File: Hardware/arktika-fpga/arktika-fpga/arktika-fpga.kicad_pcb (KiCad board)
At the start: 2 copper layers, 126 parts

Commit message: Added fuses library to project. Minor changes
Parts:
- UPER1: moved to B.Cu
- moved CPER4 325.4 mm to (64.2, 39.6), turned to 270 degrees
- moved CPER3 323.7 mm to (65.7, 39.6), turned to 270 degrees
- moved CPER1 300.4 mm to (95.5, 44.7)
- moved CPER2 300.4 mm to (92.9, 49.2)
- moved RPER1 300.4 mm to (92.8, 38.3)
- moved FUSB2 293.1 mm to (60.7, 44.5), turned to 90 degrees
- moved DUSB2 290.5 mm to (87.6, 43.6)
- moved LP1_3 153.6 mm to (49.1, 102.9), turned to 90 degrees
- moved CP6_1 153.1 mm to (48.6, 89.8), turned to 90 degrees
- moved CP1_2 149.8 mm to (50.9, 89.8), turned to 90 degrees
- moved DP3 146.5 mm to (53.6, 97.3), turned to 90 degrees
- moved CP4_1 146.2 mm to (53.5, 92.5), turned to 90 degrees
- moved CP4_3 143.2 mm to (56.0, 97.5), turned to 90 degrees
- moved CP7 142.9 mm to (55.9, 92.5), turned to 90 degrees
- moved RP2 141.0 mm to (58.3, 104.5), turned to 90 degrees
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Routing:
- net Net-(FUSB2-Pad2): track 0.00 -> 4.83 mm
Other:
- net class Default: clearance 0.2 -> 0.05
- rule trace_clearance: 0.2 -> 0.05
- rule trace_min: 0.2 -> 0.125

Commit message: Misc schematic changes. Preliminary layout almost complete
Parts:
- removed CP6: 10n, Capacitors_SMD:C_0603_HandSoldering
- removed JP1: Conn_01x03, Pin_Headers:Pin_Header_Straight_1x03_Pitch2.54mm
- added CP7_1: 10n, Capacitor_SMD:C_0603_1608Metric_Pad1.05x0.95mm_HandSolder, F.Cu at (187.4, 100.8)
- added CP7_2: 10n, Capacitor_SMD:C_0603_1608Metric_Pad1.05x0.95mm_HandSolder, F.Cu at (159.5, 84.8)
- added CP7_3: 10n, Capacitor_SMD:C_0603_1608Metric_Pad1.05x0.95mm_HandSolder, F.Cu at (177.4, 107.2)
- added JPUP6_2: SolderJumper_2_Open, Jumper:SolderJumper-2_P1.3mm_Open_RoundedPad1.0x1.5mm, F.Cu at (157.5, 103.3)
- added JUP6_1: SolderJumper_2_Open, Jumper:SolderJumper-2_P1.3mm_Open_RoundedPad1.0x1.5mm, F.Cu at (157.5, 100.8)
- A1: footprint Modules:Arduino_UNO_R3 -> Module:Arduino_UNO_R3_WithMountingHoles
- CCP5_2, CP1_2, CP1_3, CP2_2, CP2_3, CP3_2, CP3_3, CP4_2, CP4_3, CP5_3, CP6_2, CP6_3, CUP2, CUP4, CUP7, CUP9: footprint Capacitors_SMD:C_0603_HandSoldering -> Capacitor_SMD:C_0603_1608Metric_Pad1.05x0.95mm_HandSolder; moved to B.Cu
- CIN1, CP1_1, CP2_1, CP3_1, CP4_1, CP5_1, CP6_1, CPER1, CPER2, CPER3, CPER4, CUP1, CUP10, CUP11, CUP3, CUP5, CUP6, CUP8_1, CUP8_2: footprint Capacitors_SMD:C_0603_HandSoldering -> Capacitor_SMD:C_0603_1608Metric_Pad1.05x0.95mm_HandSolder
- CP10_1: renamed from CP9_1; footprint Capacitors_SMD:C_0603_HandSoldering -> Capacitor_SMD:C_0603_1608Metric_Pad1.05x0.95mm_HandSolder
- CP10_2: renamed from CP10_1; footprint Capacitors_SMD:C_0603_HandSoldering -> Capacitor_SMD:C_0603_1608Metric_Pad1.05x0.95mm_HandSolder
- CP11_1: renamed from CP9_2; footprint Capacitors_SMD:C_0603_HandSoldering -> Capacitor_SMD:C_0603_1608Metric_Pad1.05x0.95mm_HandSolder
- CP11_2: renamed from CP10_2; footprint Capacitors_SMD:C_0603_HandSoldering -> Capacitor_SMD:C_0603_1608Metric_Pad1.05x0.95mm_HandSolder
- CP8: renamed from CP7; footprint Capacitors_SMD:C_0603_HandSoldering -> Capacitor_SMD:C_0603_1608Metric_Pad1.05x0.95mm_HandSolder
- CP9: renamed from CP8; footprint Capacitors_SMD:C_0603_HandSoldering -> Capacitor_SMD:C_0603_1608Metric_Pad1.05x0.95mm_HandSolder
- D0, D1, D2, D3, D4, D5, D6, D7, DP3, DUP1, DUP2, DUP3: footprint LEDs:LED_0603_HandSoldering -> LED_SMD:LED_0603_1608Metric_Pad1.05x0.95mm_HandSolder
- DP1, DP2: footprint Diodes_SMD:D_SMA-SMB_Universal_Handsoldering -> Diode_SMD:D_SMA-SMB_Universal_Handsoldering
- DUSB1, DUSB2: footprint TO_SOT_Packages_SMD:SOT-143 -> Package_TO_SOT_SMD:SOT-143
- FP1, FUSB1, FUSB2: footprint Fuses:Fuse_1812_4532Metric -> Fuse:Fuse_1812_4532Metric_Pad1.30x3.40mm_HandSolder
- JP2: moved to B.Cu
- JUP9: footprint Pin_Headers:Pin_Header_Straight_1x07_Pitch2.54mm -> Connector_PinHeader_2.54mm:PinHeader_1x07_P2.54mm_Horizontal
- LP1_1: footprint Inductors_SMD:L_1206_HandSoldering -> Inductor_SMD:L_1206_3216Metric_Pad1.42x1.75mm_HandSolder
- LP1_2, LP1_3: footprint Inductors_SMD:L_1206_HandSoldering -> Inductor_SMD:L_1206_3216Metric_Pad1.42x1.75mm_HandSolder; moved to B.Cu
- PMODA_1, PMODA_2: footprint Pin_Headers:Pin_Header_Angled_2x06_Pitch2.54mm -> Connector_PinHeader_2.54mm:PinHeader_2x06_P2.54mm_Horizontal
- PMODB_1, PMODB_2: footprint Pin_Headers:Pin_Header_Angled_2x04_Pitch2.54mm -> Connector_PinHeader_2.54mm:PinHeader_2x04_P2.54mm_Horizontal
- PMODC_1, PMODC_2: footprint Pin_Headers:Pin_Header_Angled_1x06_Pitch2.54mm -> Connector_PinHeader_2.54mm:PinHeader_1x06_P2.54mm_Horizontal
- PSH0, PSH1, PSH2, PSH3: footprint Buttons_Switches_SMD:SW_SPST_PTS645 -> Button_Switch_SMD:SW_SPST_PTS645
- RP1_1, RP1_2, RP2, RPER1, RUP1, RUP2, RUP3, RUP7_1, RUP8: footprint Resistors_SMD:R_0603_HandSoldering -> Resistor_SMD:R_0603_1608Metric_Pad1.05x0.95mm_HandSolder
- RPER2: footprint Resistors_SMD:R_Array_Convex_4x0603 -> Resistor_SMD:R_Array_Convex_4x0603; moved to B.Cu
- RPER3, RPER4, RPER5, RPER6: footprint Resistors_SMD:R_Array_Convex_4x0603 -> Resistor_SMD:R_Array_Convex_4x0603
- RUP4, RUP5, RUP6, RUP7, RUP7_2, RUP7_3, RUP7_4: footprint Resistors_SMD:R_0603_HandSoldering -> Resistor_SMD:R_0603_1608Metric_Pad1.05x0.95mm_HandSolder; moved to B.Cu
- SW[7..0]1: footprint Buttons_Switches_SMD:SW_DIP_x8_W8.61mm_Slide_LowProfile -> Button_Switch_SMD:SW_DIP_SPSTx08_Slide_6.7x21.88mm_W8.61mm_P2.54mm_LowProfile
- UP1: footprint TO_SOT_Packages_SMD:SOT-223-3_TabPin2 -> Package_TO_SOT_SMD:SOT-223-3_TabPin2
- UP2, UP3: footprint TO_SOT_Packages_SMD:SOT-23 -> Package_TO_SOT_SMD:SOT-23; moved to B.Cu
- UPER1: footprint Housings_DFN_QFN:QFN-28-1EP_4x4mm_Pitch0.4mm -> Package_DFN_QFN:QFN-28-1EP_4x4mm_P0.4mm_EP2.6x2.6mm; moved to F.Cu
- UPER2: footprint Housings_SOIC:SOIC-14_3.9x8.7mm_Pitch1.27mm -> Package_SO:SOIC-14_3.9x8.7mm_P1.27mm
- UUP1: footprint Housings_QFP:LQFP-48_7x7mm_Pitch0.5mm -> Package_QFP:LQFP-48-1EP_7x7mm_P0.5mm_EP3.6x3.6mm
- UUP2: footprint TO_SOT_Packages_SMD:SOT-23-6_Handsoldering -> Package_TO_SOT_SMD:SOT-23-6_Handsoldering; moved to B.Cu
- UUP3: footprint Housings_QFP:TQFP-144_20x20mm_Pitch0.5mm -> Package_QFP:TQFP-144_20x20mm_P0.5mm
- UUP4: footprint Housings_SOIC:SOIC-8_3.9x4.9mm_Pitch1.27mm -> Package_SO:SOIC-8_3.9x4.9mm_P1.27mm
- YUP1: footprint Crystals:Crystal_SMD_3225-4pin_3.2x2.5mm_HandSoldering -> Crystal:Crystal_SMD_3225-4Pin_3.2x2.5mm_HandSoldering
- moved CUP5 268.2 mm to (106.8, 113.0), turned to 270 degrees
- moved CUP8_1 264.3 mm to (106.2, 104.0), turned to 90 degrees
- moved CUP10 254.4 mm to (109.4, 124.5), turned to 270 degrees
- moved RPER6 249.4 mm to (149.8, 116.5), turned to 90 degrees
- moved RPER5 247.2 mm to (145.6, 116.5), turned to 90 degrees
- moved CUP6 245.9 mm to (110.3, 102.9), turned to 180 degrees
- moved CUP9 242.6 mm to (105.5, 101.0), turned to 180 degrees
- moved JUP5_1 239.4 mm to (96.8, 100.3)
- moved D7 238.2 mm to (145.2, 123.4)
- moved D6 237.5 mm to (147.6, 123.4)
- moved JUP5_2 236.7 mm to (94.9, 102.5)
- moved D5 236.7 mm to (150.2, 123.4)
- moved D4 235.9 mm to (152.7, 123.4)
- moved D3 235.0 mm to (155.3, 123.4)
- moved RPER4 235.0 mm to (159.1, 132.0)
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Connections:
- net /Power/D+ renamed /D+
- net /Power/D- renamed /D-
- net Net-(JUP5_1-Pad2) renamed /USB AND PROG/D'-
- net Net-(JUP5_2-Pad2) renamed /USB AND PROG/D'+
- net Net-(UUP3-Pad110) renamed /FPGA_IO/EXT1
- A1 pad 10: /FPGA_IO/ADC_CH1 -> ADC_CH1
- A1 pad 11: /FPGA_IO/ADC_CH2 -> ADC_CH2
- A1 pad 12: /FPGA_IO/ADC_CH3 -> ADC_CH3
- A1 pad 9: /FPGA_IO/ADC_CH0 -> ADC_CH0
- CP10_1 pad 2: /Power/GNDPLL0 -> /GNDPLL1
- CP10_2 pad 2: /Power/GNDPLL0 -> /GNDPLL1
- CP11_1 pad 2: /Power/GNDPLL1 -> /GNDPLL0
- CP11_2 pad 2: /Power/GNDPLL1 -> /GNDPLL0
- CUP4 pad 1: Net-(CUP4-Pad1) -> /VCC3V3
- CUP6 pad 1: Net-(CUP4-Pad1) -> /VCC3V3
- DP2 pad 2: Net-(DP2-Pad2) -> /Power/Vbus
- DUP1 pad 1: /USB AND PROG/C9 -> /USB AND PROG/C8'
- DUP2 pad 1: /USB AND PROG/C8 -> /USB AND PROG/C9'
- FUSB1 pad 1: Net-(DP2-Pad2) -> /Power/Vbus
- JUP6 pad 17: Net-(JUP6-Pad17) -> /USB AND PROG/C8'
- JUP6 pad 18: Net-(JUP6-Pad18) -> /USB AND PROG/C9'
- JUP7_1 pad 7: Net-(JUP6-Pad17) -> /USB AND PROG/C8'
- JUP7_1 pad 8: Net-(JUP6-Pad18) -> /USB AND PROG/C9'
- JUP9 pad 1: /USB AND PROG/FLASH_CS -> /USB AND PROG/flash_~RST
- JUP9 pad 2: /USB AND PROG/ICE_SCK -> /USB AND PROG/flash_~WP
- JUP9 pad 3: /USB AND PROG/FLASH_MOSI -> /USB AND PROG/FLASH_MISO
- JUP9 pad 4: /USB AND PROG/FLASH_MISO -> /USB AND PROG/FLASH_MOSI
- JUP9 pad 5: /USB AND PROG/flash_~WP -> /USB AND PROG/ICE_SCK
- JUP9 pad 6: /USB AND PROG/flash_~RST -> /USB AND PROG/FLASH_CS
- PSH0 pad 2: /FPGA_PERIPHS/PSH0 -> /FPGA_IO/PSH0
- PSH1 pad 2: /FPGA_PERIPHS/PSH1 -> /FPGA_IO/PSH1
- PSH2 pad 2: /FPGA_PERIPHS/PSH2 -> /FPGA_IO/PSH2
- PSH3 pad 2: /FPGA_PERIPHS/PSH3 -> /FPGA_IO/PSH3
- RPER2 pad 1: /FPGA_PERIPHS/PSH0 -> /FPGA_IO/PSH0
- RPER2 pad 2: /FPGA_PERIPHS/PSH1 -> /FPGA_IO/PSH1
- RPER2 pad 3: /FPGA_PERIPHS/PSH2 -> /FPGA_IO/PSH2
- RPER2 pad 4: /FPGA_PERIPHS/PSH3 -> /FPGA_IO/PSH3
- RPER3 pad 1: /FPGA_PERIPHS/SW7 -> /FPGA_IO/SW7
- RPER3 pad 2: /FPGA_PERIPHS/SW6 -> /FPGA_IO/SW6
- RPER3 pad 3: /FPGA_PERIPHS/SW5 -> /FPGA_IO/SW5
- RPER3 pad 4: /FPGA_PERIPHS/SW4 -> /FPGA_IO/SW4
- RPER4 pad 1: /FPGA_PERIPHS/SW3 -> /FPGA_IO/SW3
- RPER4 pad 2: /FPGA_PERIPHS/SW2 -> /FPGA_IO/SW2
- RPER4 pad 3: /FPGA_PERIPHS/SW1 -> /FPGA_IO/SW1
- RPER4 pad 4: /FPGA_PERIPHS/SW0 -> /FPGA_IO/SW0
- RPER5 pad 5: /FPGA_PERIPHS/LED4 -> /FPGA_IO/LED4
- RPER5 pad 6: /FPGA_PERIPHS/LED5 -> /FPGA_IO/LED5
- RPER5 pad 7: /FPGA_PERIPHS/LED6 -> /FPGA_IO/LED6
- RPER5 pad 8: /FPGA_PERIPHS/LED7 -> /FPGA_IO/LED7
- RPER6 pad 5: /FPGA_PERIPHS/LED0 -> /FPGA_IO/LED0
- RPER6 pad 6: /FPGA_PERIPHS/LED1 -> /FPGA_IO/LED1
- RPER6 pad 7: /FPGA_PERIPHS/LED2 -> /FPGA_IO/LED2
- RPER6 pad 8: /FPGA_PERIPHS/LED3 -> /FPGA_IO/LED3
- SW[7..0]1 pad 1: /FPGA_PERIPHS/SW0 -> /FPGA_IO/SW0
- SW[7..0]1 pad 2: /FPGA_PERIPHS/SW1 -> /FPGA_IO/SW1
- SW[7..0]1 pad 3: /FPGA_PERIPHS/SW2 -> /FPGA_IO/SW2
- SW[7..0]1 pad 4: /FPGA_PERIPHS/SW3 -> /FPGA_IO/SW3
- SW[7..0]1 pad 5: /FPGA_PERIPHS/SW4 -> /FPGA_IO/SW4
- SW[7..0]1 pad 6: /FPGA_PERIPHS/SW5 -> /FPGA_IO/SW5
- SW[7..0]1 pad 7: /FPGA_PERIPHS/SW6 -> /FPGA_IO/SW6
- SW[7..0]1 pad 8: /FPGA_PERIPHS/SW7 -> /FPGA_IO/SW7
- UPER1 pad 25: /FPGA_PERIPHS/RX -> UART_RX
- UPER1 pad 26: /FPGA_PERIPHS/TX -> UART_TX
- UPER2 pad 1: /FPGA_PERIPHS/ADC_CH0 -> ADC_CH0
- UPER2 pad 10: /FPGA_PERIPHS/ADC_MISO -> ADC_MISO
- UPER2 pad 11: /FPGA_PERIPHS/ADC_CLK -> ADC_CLK
- UPER2 pad 2: /FPGA_PERIPHS/ADC_CH1 -> ADC_CH1
- UPER2 pad 3: /FPGA_PERIPHS/ADC_CH2 -> ADC_CH2
- UPER2 pad 4: /FPGA_PERIPHS/ADC_CH3 -> ADC_CH3
- UPER2 pad 8: /FPGA_PERIPHS/ADC_CS -> ADC_CS
- UPER2 pad 9: /FPGA_PERIPHS/ADC_MOSI -> ADC_MOSI
- UUP1 pad 32: Net-(JUP6-Pad17) -> /USB AND PROG/C8'
- UUP1 pad 33: Net-(JUP6-Pad18) -> /USB AND PROG/C9'
- UUP3 pad 1: Net-(UUP3-Pad1) -> /FPGA_IO/LED1
- UUP3 pad 10: Net-(UUP3-Pad10) -> /FPGA_IO/SW2
- UUP3 pad 101: Net-(UUP3-Pad101) -> /FPGA_IO/PMOD1_B_9
- UUP3 pad 102: Net-(UUP3-Pad102) -> /FPGA_IO/PMOD1_B_10
- UUP3 pad 104: Net-(UUP3-Pad104) -> /FPGA_IO/PMOD1_B_1
- UUP3 pad 105: Net-(UUP3-Pad105) -> /FPGA_IO/PMOD1_B_2
- UUP3 pad 106: Net-(UUP3-Pad106) -> /FPGA_IO/PMOD1_B_3
- UUP3 pad 107: Net-(UUP3-Pad107) -> /FPGA_IO/PMOD1_B_4
- UUP3 pad 11: Net-(UUP3-Pad11) -> /FPGA_IO/SW1
- UUP3 pad 115: Net-(UUP3-Pad115) -> /FPGA_IO/PMOD1_A_1
- UUP3 pad 116: Net-(UUP3-Pad116) -> /FPGA_IO/PMOD1_A_2
- UUP3 pad 117: Net-(UUP3-Pad117) -> /FPGA_IO/PMOD1_A_3
- UUP3 pad 118: Net-(UUP3-Pad118) -> /FPGA_IO/PMOD1_A_4
- UUP3 pad 119: Net-(UUP3-Pad119) -> /FPGA_IO/PMOD1_A_7
- UUP3 pad 12: Net-(UUP3-Pad12) -> /FPGA_IO/SW0
- UUP3 pad 120: Net-(UUP3-Pad120) -> /FPGA_IO/PMOD1_A_8
- UUP3 pad 121: Net-(UUP3-Pad121) -> /FPGA_IO/PMOD1_A_9
- UUP3 pad 122: Net-(UUP3-Pad122) -> /FPGA_IO/PMOD1_A_10
- UUP3 pad 124: Net-(UUP3-Pad124) -> /FPGA_IO/Buzzer
- UUP3 pad 127: /USB AND PROG/GNDPLL1 -> /GNDPLL0
- UUP3 pad 134: Net-(UUP3-Pad134) -> UART_RX
- UUP3 pad 135: Net-(UUP3-Pad135) -> UART_TX
- UUP3 pad 136: Net-(UUP3-Pad136) -> /FPGA_IO/LED7
- UUP3 pad 137: Net-(UUP3-Pad137) -> /FPGA_IO/LED6
- UUP3 pad 138: Net-(UUP3-Pad138) -> /FPGA_IO/LED5
- UUP3 pad 139: Net-(UUP3-Pad139) -> /FPGA_IO/LED4
- UUP3 pad 141: Net-(UUP3-Pad141) -> /FPGA_IO/LED3
- UUP3 pad 142: Net-(UUP3-Pad142) -> /FPGA_IO/LED2
- UUP3 pad 15: Net-(UUP3-Pad15) -> /FPGA_IO/ARDUINO_D13
- UUP3 pad 16: Net-(UUP3-Pad16) -> /FPGA_IO/ARDUINO_D12
- UUP3 pad 17: Net-(UUP3-Pad17) -> /FPGA_IO/ARDUINO_D11
- UUP3 pad 18: Net-(UUP3-Pad18) -> /FPGA_IO/ARDUINO_D10
- UUP3 pad 19: Net-(UUP3-Pad19) -> /FPGA_IO/ARDUINO_D9
- UUP3 pad 2: Net-(UUP3-Pad2) -> /FPGA_IO/LED0
- UUP3 pad 20: Net-(UUP3-Pad20) -> /FPGA_IO/ARDUINO_D8
- UUP3 pad 21: Net-(UUP3-Pad21) -> /FPGA_IO/ARDUINO_D7
- UUP3 pad 22: Net-(UUP3-Pad22) -> /FPGA_IO/ARDUINO_D6
- UUP3 pad 23: Net-(UUP3-Pad23) -> /FPGA_IO/ARDUINO_D5
- UUP3 pad 24: Net-(UUP3-Pad24) -> /FPGA_IO/ARDUINO_D4
- UUP3 pad 25: Net-(UUP3-Pad25) -> /FPGA_IO/ARDUINO_D3
- UUP3 pad 26: Net-(UUP3-Pad26) -> /FPGA_IO/ARDUINO_D2
- UUP3 pad 28: Net-(UUP3-Pad28) -> /FPGA_IO/ARDUINO_D1
- UUP3 pad 29: Net-(UUP3-Pad29) -> /FPGA_IO/ARDUINO_D0
- UUP3 pad 3: Net-(UUP3-Pad3) -> /FPGA_IO/SW7
- UUP3 pad 31: Net-(UUP3-Pad31) -> /FPGA_IO/PSH0
- UUP3 pad 32: Net-(UUP3-Pad32) -> /FPGA_IO/PSH1
- UUP3 pad 33: Net-(UUP3-Pad33) -> /FPGA_IO/PSH2
- UUP3 pad 34: Net-(UUP3-Pad34) -> /FPGA_IO/PSH3
- UUP3 pad 4: Net-(UUP3-Pad4) -> /FPGA_IO/SW6
- UUP3 pad 49: Net-(UUP3-Pad49) -> /FPGA_IO/OSC_OUT
- UUP3 pad 52: Net-(UUP3-Pad52) -> ADC_CH0
- UUP3 pad 53: /USB AND PROG/GNDPLL0 -> /GNDPLL1
- UUP3 pad 55: Net-(UUP3-Pad55) -> ADC_CH1
- UUP3 pad 56: Net-(UUP3-Pad56) -> ADC_CH2
- UUP3 pad 60: Net-(UUP3-Pad60) -> ADC_CH3
- UUP3 pad 61: Net-(UUP3-Pad61) -> ADC_CS
- UUP3 pad 62: Net-(UUP3-Pad62) -> ADC_MOSI
- UUP3 pad 63: Net-(UUP3-Pad63) -> ADC_MISO
- UUP3 pad 64: Net-(UUP3-Pad64) -> ADC_CLK
- UUP3 pad 7: Net-(UUP3-Pad7) -> /FPGA_IO/SW5
- UUP3 pad 73: Net-(UUP3-Pad73) -> /FPGA_IO/PMOD2_B_3
- UUP3 pad 74: Net-(UUP3-Pad74) -> /FPGA_IO/PMOD2_A_1
- UUP3 pad 75: Net-(UUP3-Pad75) -> /FPGA_IO/PMOD2_B_4
- UUP3 pad 76: Net-(UUP3-Pad76) -> /FPGA_IO/PMOD2_B_2
- UUP3 pad 78: Net-(UUP3-Pad78) -> /FPGA_IO/PMOD2_A_3
- UUP3 pad 79: Net-(UUP3-Pad79) -> /FPGA_IO/PMOD2_A_1
- UUP3 pad 8: Net-(UUP3-Pad8) -> /FPGA_IO/SW4
- UUP3 pad 80: Net-(UUP3-Pad80) -> /FPGA_IO/PMOD2_A_4
- UUP3 pad 81: Net-(UUP3-Pad81) -> /FPGA_IO/PMOD2_A_2
- UUP3 pad 88: Net-(UUP3-Pad88) -> /FPGA_IO/PMOD3_A_4
- UUP3 pad 9: Net-(UUP3-Pad9) -> /FPGA_IO/SW3
- UUP3 pad 90: Net-(UUP3-Pad90) -> /FPGA_IO/PMOD3_A_3
- UUP3 pad 91: Net-(UUP3-Pad91) -> /FPGA_IO/PMOD3_A_2
- UUP3 pad 93: /FPGA_IO/OSC_OUT -> /FPGA_IO/PMOD3_A_1
- UUP3 pad 94: Net-(UUP3-Pad94) -> /FPGA_IO/PMOD3_B_4
- UUP3 pad 95: Net-(UUP3-Pad95) -> /FPGA_IO/PMOD3_B_3
- UUP3 pad 96: Net-(UUP3-Pad96) -> /FPGA_IO/PMOD3_B_2
- UUP3 pad 97: Net-(UUP3-Pad97) -> /FPGA_IO/PMOD3_B_1
- UUP3 pad 98: Net-(UUP3-Pad98) -> /FPGA_IO/PMOD1_B_7
- UUP3 pad 99: Net-(UUP3-Pad99) -> /FPGA_IO/PMOD1_B_8
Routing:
- net /VCC3V3: track 0.00 -> 426.3 mm, vias 0 -> 15
- net /Power/VCC_CORE: track 0.00 -> 177.5 mm, vias 0 -> 6
- net /Power/VCC1.2_PLL: track 0.00 -> 157.6 mm, vias 0 -> 2
- net /D-: track 0.00 -> 107.5 mm, vias 0 -> 2
- net /D+: track 0.00 -> 106.6 mm, vias 0 -> 4
- net /USB AND PROG/FLASH_MOSI: track 0.00 -> 76.9 mm, vias 0 -> 2
- net /USB AND PROG/ICE_SO: track 0.00 -> 59.8 mm, vias 0 -> 1
- net /USB AND PROG/FLASH_MISO: track 0.00 -> 55.9 mm, vias 0 -> 1
- net /USB AND PROG/ICE_SI: track 0.00 -> 49.5 mm, vias 0 -> 1
- net /USB AND PROG/ICE_SCK: track 0.00 -> 44.0 mm, vias 0 -> 2
- net /FPGA_PERIPHS/D-: track 0.00 -> 41.7 mm, vias 0 -> 3
- net /FPGA_PERIPHS/D+: track 0.00 -> 41.3 mm, vias 0 -> 2
- net /USB AND PROG/flash_~RST: track 0.00 -> 40.1 mm, vias 0 -> 1
- net /FPGA_IO/SW1: track 0.00 -> 39.4 mm, vias 0 -> 2
- net /FPGA_IO/SW2: track 0.00 -> 37.6 mm, vias 0 -> 2
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- added copper zone on F.Cu, net /Power/Vbus
- added copper zone on F.Cu, net /VCC3V3
- added copper zone on F.Cu, net /VCC5V
- added copper zone on F.Cu, net /VIN
- added copper zone on F.Cu, net GND
- added copper zone on B.Cu, net Net-(CCP5_2-Pad1)
- added copper zone on F.Cu, net Net-(CP3_1-Pad1)
- added copper zone on B.Cu, net Net-(CP3_3-Pad1)
- added copper zone on F.Cu, net Net-(DP1-Pad2)
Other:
- board outline added: 131.8 x 90.1 mm
- copper layers 2 -> 4
- rule pad_to_mask_clearance: 0.05 -> 0
- rule via_min_size: 0.4 -> 0.6

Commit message: Major routing updates. Did work on silkscreen. Optimized io placing. Misc changes
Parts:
- A1: footprint Module:Arduino_UNO_R3_WithMountingHoles -> Module:Arduino_UNO_R3
- JUP6: value Conn_01x18 -> Conn_02x10_Odd_Even; footprint Pin_Headers:Pin_Header_Straight_1x18_Pitch2.54mm -> Connector_PinHeader_2.54mm:PinHeader_2x10_P2.54mm_Vertical
- PMODA_1, PMODA_2: value Conn_02x06_Top_Bottom -> Conn_02x06_Odd_Even
- moved BPER1 97.5 mm to (229.3, 93.7)
- moved JUP6 36.5 mm to (132.1, 101.0)
- moved RUP7_4 6.12 mm to (119.5, 121.3), turned to 180 degrees
- moved RUP7_2 4.88 mm to (119.5, 131.0)
- moved RUP7_1 4.88 mm to (114.2, 127.5)
- moved CUP10 4.88 mm to (114.2, 124.0)
- moved UUP4 4.88 mm to (117.7, 125.9)
- moved PMODB_2 2.62 mm to (198.6, 64.3)
- moved PMODA_1 2.45 mm to (88.5, 64.3)
- moved PMODA_2 2.45 mm to (111.7, 64.3)
- moved PMODB_1 2.45 mm to (181.0, 64.3)
- moved PMODC_1 2.45 mm to (134.8, 61.7)
- moved PMODC_2 2.45 mm to (157.9, 61.7)
- moved CP8 2.05 mm to (162.5, 79.9)
- moved CP11_1 0.58 mm to (157.6, 93.6)
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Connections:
- net Net-(JUP6-Pad1) renamed /USB AND PROG/ADBUS0
- net Net-(JUP6-Pad16) renamed /USB AND PROG/ACBUS7
- CP7_3 pad 1: Net-(CP7_3-Pad1) -> /Power/VCC_CORE
- CUP11 pad 1: /FPGA_IO/3V3 -> /VCC3V3
- JUP6 pad 10: Net-(JUP6-Pad10) -> /USB AND PROG/ACBUS4
- JUP6 pad 11: Net-(JUP6-Pad11) -> /USB AND PROG/ADBUS5
- JUP6 pad 12: Net-(JUP6-Pad12) -> /USB AND PROG/ACBUS5
- JUP6 pad 13: Net-(JUP6-Pad13) -> /USB AND PROG/ADBUS6
- JUP6 pad 14: Net-(JUP6-Pad14) -> /USB AND PROG/ACBUS6
- JUP6 pad 15: Net-(JUP6-Pad15) -> /USB AND PROG/ADBUS7
- JUP6 pad 2: Net-(JUP6-Pad2) -> /USB AND PROG/ACBUS0
- JUP6 pad 3: Net-(JUP6-Pad3) -> /USB AND PROG/ADBUS1
- JUP6 pad 4: Net-(JUP6-Pad4) -> /USB AND PROG/ACBUS1
- JUP6 pad 5: Net-(JUP6-Pad5) -> /USB AND PROG/ADBUS2
- JUP6 pad 6: Net-(JUP6-Pad6) -> /USB AND PROG/ACBUS2
- JUP6 pad 7: Net-(JUP6-Pad7) -> /USB AND PROG/ADBUS3
- JUP6 pad 8: Net-(JUP6-Pad8) -> /USB AND PROG/ACBUS3
- JUP6 pad 9: Net-(JUP6-Pad9) -> /USB AND PROG/ADBUS4
- JUP7_1 pad 2: Net-(JUP6-Pad2) -> /USB AND PROG/ADBUS1
- JUP7_1 pad 3: Net-(JUP6-Pad3) -> /USB AND PROG/ADBUS2
- JUP7_1 pad 4: Net-(JUP6-Pad5) -> /USB AND PROG/ADBUS4
- JUP7_1 pad 5: Net-(JUP6-Pad7) -> /USB AND PROG/ADBUS6
- JUP7_1 pad 6: Net-(JUP6-Pad8) -> /USB AND PROG/ADBUS7
- PMODA_1 pad 10: /FPGA_IO/PMOD1_A_10 -> GND
- PMODA_1 pad 11: GND -> /VCC3V3
- PMODA_1 pad 12: /FPGA_IO/3V3 -> /VCC3V3
- PMODA_1 pad 2: /FPGA_IO/PMOD1_A_2 -> /FPGA_IO/PMOD1_A_7
- PMODA_1 pad 3: /FPGA_IO/PMOD1_A_3 -> /FPGA_IO/PMOD1_A_2
- PMODA_1 pad 4: /FPGA_IO/PMOD1_A_4 -> /FPGA_IO/PMOD1_A_8
- PMODA_1 pad 5: GND -> /FPGA_IO/PMOD1_A_3
- PMODA_1 pad 6: /FPGA_IO/3V3 -> /FPGA_IO/PMOD1_A_9
- PMODA_1 pad 7: /FPGA_IO/PMOD1_A_7 -> /FPGA_IO/PMOD1_A_4
- PMODA_1 pad 8: /FPGA_IO/PMOD1_A_8 -> /FPGA_IO/PMOD1_A_10
- PMODA_1 pad 9: /FPGA_IO/PMOD1_A_9 -> GND
- PMODA_2 pad 10: /FPGA_IO/PMOD1_B_10 -> GND
- PMODA_2 pad 11: GND -> /VCC3V3
- PMODA_2 pad 12: /FPGA_IO/3V3 -> /VCC3V3
- PMODA_2 pad 2: /FPGA_IO/PMOD1_B_2 -> /FPGA_IO/PMOD1_B_7
- PMODA_2 pad 3: /FPGA_IO/PMOD1_B_3 -> /FPGA_IO/PMOD1_B_2
- PMODA_2 pad 4: /FPGA_IO/PMOD1_B_4 -> /FPGA_IO/PMOD1_B_8
- PMODA_2 pad 5: GND -> /FPGA_IO/PMOD1_B_3
- PMODA_2 pad 6: /FPGA_IO/3V3 -> /FPGA_IO/PMOD1_B_9
- PMODA_2 pad 7: /FPGA_IO/PMOD1_B_7 -> /FPGA_IO/PMOD1_B_4
- PMODA_2 pad 8: /FPGA_IO/PMOD1_B_8 -> /FPGA_IO/PMOD1_B_10
- PMODA_2 pad 9: /FPGA_IO/PMOD1_B_9 -> GND
- PMODB_1 pad 7: /FPGA_IO/3V3 -> /VCC3V3
- PMODB_1 pad 8: /FPGA_IO/3V3 -> /VCC3V3
- PMODB_2 pad 1: /FPGA_IO/PMOD2_A_1 -> /FPGA_IO/PMOD2_B_1
- PMODB_2 pad 7: /FPGA_IO/3V3 -> /VCC3V3
- PMODB_2 pad 8: /FPGA_IO/3V3 -> /VCC3V3
- PMODC_1 pad 6: /FPGA_IO/3V3 -> /VCC3V3
- PMODC_2 pad 6: /FPGA_IO/3V3 -> /VCC3V3
- UUP1 pad 14: Net-(JUP6-Pad2) -> /USB AND PROG/ADBUS1
- UUP1 pad 15: Net-(JUP6-Pad3) -> /USB AND PROG/ADBUS2
- UUP1 pad 16: Net-(JUP6-Pad4) -> /USB AND PROG/ADBUS3
- UUP1 pad 17: Net-(JUP6-Pad5) -> /USB AND PROG/ADBUS4
- UUP1 pad 18: Net-(JUP6-Pad6) -> /USB AND PROG/ADBUS5
- UUP1 pad 19: Net-(JUP6-Pad7) -> /USB AND PROG/ADBUS6
- UUP1 pad 20: Net-(JUP6-Pad8) -> /USB AND PROG/ADBUS7
- UUP1 pad 21: Net-(JUP6-Pad9) -> /USB AND PROG/ACBUS0
- UUP1 pad 25: Net-(JUP6-Pad10) -> /USB AND PROG/ACBUS1
- UUP1 pad 26: Net-(JUP6-Pad11) -> /USB AND PROG/ACBUS2
- UUP1 pad 27: Net-(JUP6-Pad12) -> /USB AND PROG/ACBUS3
- UUP1 pad 28: Net-(JUP6-Pad13) -> /USB AND PROG/ACBUS4
- UUP1 pad 29: Net-(JUP6-Pad14) -> /USB AND PROG/ACBUS5
- UUP1 pad 30: Net-(JUP6-Pad15) -> /USB AND PROG/ACBUS6
- UUP3 pad 102: /FPGA_IO/PMOD1_B_10 -> /FPGA_IO/PMOD1_B_3
- UUP3 pad 104: /FPGA_IO/PMOD1_B_1 -> /FPGA_IO/PMOD1_B_8
- UUP3 pad 106: /FPGA_IO/PMOD1_B_3 -> /FPGA_IO/PMOD1_B_7
- UUP3 pad 107: /FPGA_IO/PMOD1_B_4 -> /FPGA_IO/PMOD1_B_1
- UUP3 pad 115: /FPGA_IO/PMOD1_A_1 -> /FPGA_IO/PMOD1_A_10
- UUP3 pad 116: /FPGA_IO/PMOD1_A_2 -> /FPGA_IO/PMOD1_A_4
- UUP3 pad 117: /FPGA_IO/PMOD1_A_3 -> /FPGA_IO/PMOD1_A_9
- UUP3 pad 118: /FPGA_IO/PMOD1_A_4 -> /FPGA_IO/PMOD1_A_3
- UUP3 pad 119: /FPGA_IO/PMOD1_A_7 -> /FPGA_IO/PMOD1_A_8
- UUP3 pad 120: /FPGA_IO/PMOD1_A_8 -> /FPGA_IO/PMOD1_A_2
- UUP3 pad 121: /FPGA_IO/PMOD1_A_9 -> /FPGA_IO/PMOD1_A_7
- UUP3 pad 122: /FPGA_IO/PMOD1_A_10 -> /FPGA_IO/PMOD1_A_1
- UUP3 pad 73: /FPGA_IO/PMOD2_B_3 -> Net-(UUP3-Pad73)
- UUP3 pad 74: /FPGA_IO/PMOD2_A_1 -> Net-(UUP3-Pad74)
- UUP3 pad 75: /FPGA_IO/PMOD2_B_4 -> Net-(UUP3-Pad75)
- UUP3 pad 76: /FPGA_IO/PMOD2_B_2 -> /FPGA_IO/PMOD2_B_3
- UUP3 pad 78: /FPGA_IO/PMOD2_A_3 -> /FPGA_IO/PMOD2_B_1
- UUP3 pad 79: /FPGA_IO/PMOD2_A_1 -> /FPGA_IO/PMOD2_B_4
- UUP3 pad 80: /FPGA_IO/PMOD2_A_4 -> /FPGA_IO/PMOD2_B_2
- UUP3 pad 81: /FPGA_IO/PMOD2_A_2 -> /FPGA_IO/PMOD2_A_3
- UUP3 pad 82: Net-(UUP3-Pad82) -> /FPGA_IO/PMOD2_A_1
- UUP3 pad 83: Net-(UUP3-Pad83) -> /FPGA_IO/PMOD2_A_4
- UUP3 pad 84: Net-(UUP3-Pad84) -> /FPGA_IO/PMOD2_A_2
- UUP3 pad 85: Net-(UUP3-Pad85) -> /FPGA_IO/ARDUINO_RESET
- UUP3 pad 87: Net-(UUP3-Pad87) -> /FPGA_IO/ARDUINO_EXTRA_1
- UUP3 pad 88: /FPGA_IO/PMOD3_A_4 -> /FPGA_IO/PMOD3_B_4
- UUP3 pad 90: /FPGA_IO/PMOD3_A_3 -> /FPGA_IO/PMOD3_B_3
- UUP3 pad 91: /FPGA_IO/PMOD3_A_2 -> /FPGA_IO/PMOD3_B_2
- UUP3 pad 93: /FPGA_IO/PMOD3_A_1 -> /FPGA_IO/PMOD3_B_1
- UUP3 pad 94: /FPGA_IO/PMOD3_B_4 -> /FPGA_IO/PMOD3_A_4
- UUP3 pad 95: /FPGA_IO/PMOD3_B_3 -> /FPGA_IO/PMOD3_A_3
- UUP3 pad 96: /FPGA_IO/PMOD3_B_2 -> /FPGA_IO/PMOD3_A_2
- UUP3 pad 97: /FPGA_IO/PMOD3_B_1 -> /FPGA_IO/PMOD3_A_1
- UUP3 pad 98: /FPGA_IO/PMOD1_B_7 -> /FPGA_IO/PMOD1_B_10
- UUP3 pad 99: /FPGA_IO/PMOD1_B_8 -> /FPGA_IO/PMOD1_B_4
- XUP1 pad 4: /FPGA_IO/3V3 -> /VCC3V3
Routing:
- net /VCC3V3: track 426.3 -> 605.8 mm, vias 15 -> 20
- net /VCC5V: track 7.56 -> 156.1 mm, vias 0 -> 2
- net /VIN: track 5.79 -> 143.5 mm, vias 0 -> 2
- net /FPGA_IO/PMOD1_A_7: track 0.00 -> 98.6 mm, vias 0 -> 1
- net /FPGA_IO/PMOD1_A_1: track 0.00 -> 97.6 mm, vias 0 -> 1
- net /FPGA_IO/PMOD1_A_8: track 0.00 -> 94.9 mm, vias 0 -> 1
- net /FPGA_IO/PMOD1_A_2: track 0.00 -> 93.6 mm, vias 0 -> 1
- net /USB AND PROG/FLASH_CS: track 19.7 -> 112.3 mm, vias 1 -> 5
- net /FPGA_IO/PMOD1_A_9: track 0.00 -> 91.3 mm, vias 0 -> 2
- net /FPGA_IO/PMOD1_A_3: track 0.00 -> 90.0 mm, vias 0 -> 1
- net /FPGA_IO/PMOD1_A_10: track 0.00 -> 88.8 mm, vias 0 -> 2
- net UART_TX: track 0.00 -> 88.4 mm
- net /FPGA_IO/PMOD1_A_4: track 0.00 -> 87.2 mm, vias 0 -> 2
- net UART_RX: track 0.00 -> 86.8 mm, vias 0 -> 2
- net /USB AND PROG/ICE_SCK: track 44.0 -> 116.4 mm, vias 2 -> 5
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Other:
- board size 131.8 x 90.1 mm -> 131.8 x 81.3 mm
- board text added: "FTDI Breakout"
- board text added: "For programming ICE For programming Flash"
- board text added: "GND C8 D7 D6 D5 D4 D3 D2 D1 D0"
- board text added: "GND C9 C7 C6 C5 C4 C3 C2 C1 C0"
- board text added: "GND ~CS SCK MOSI MISO ~WP ~RST"
- board text added: "Jumper for normal operation"
- board text added: "SPI FLASH"
- board text added: "USB PROG"
- board text added: "USB UART"

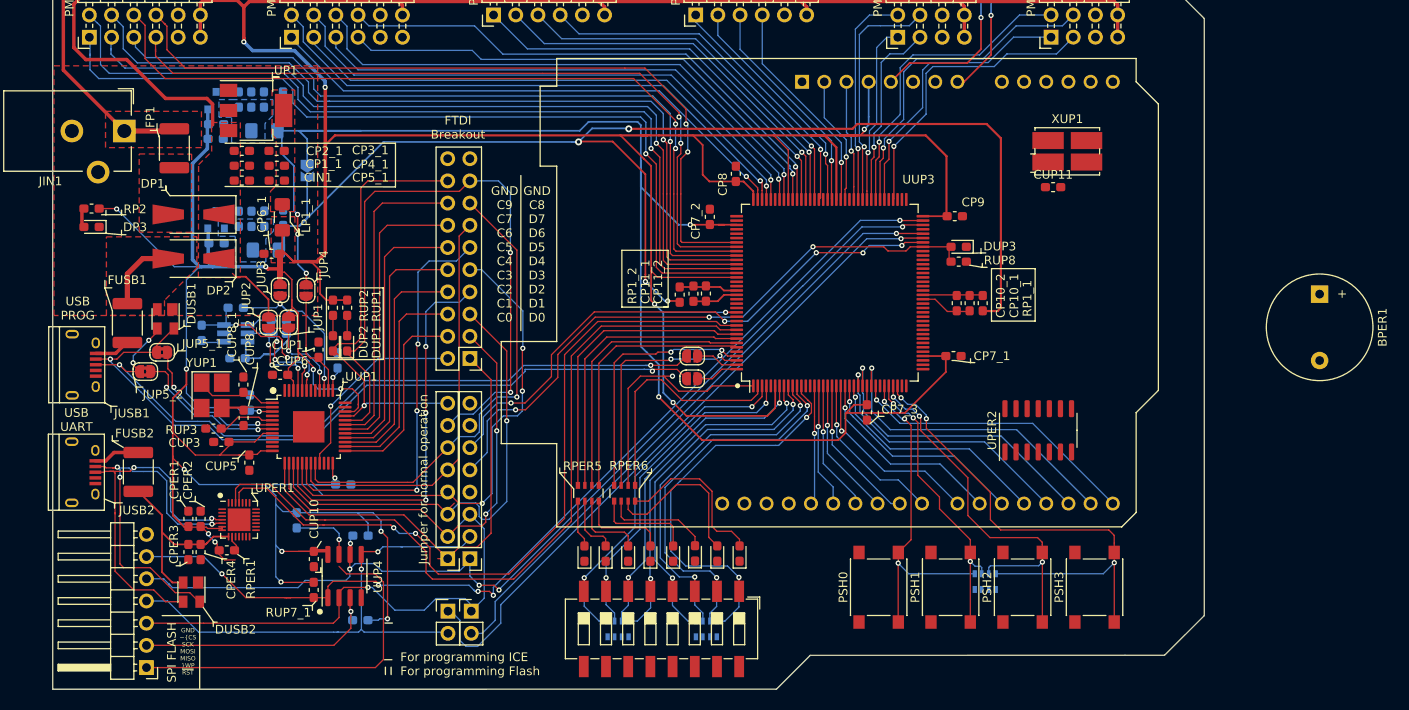
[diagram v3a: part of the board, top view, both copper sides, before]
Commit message: Added more IO
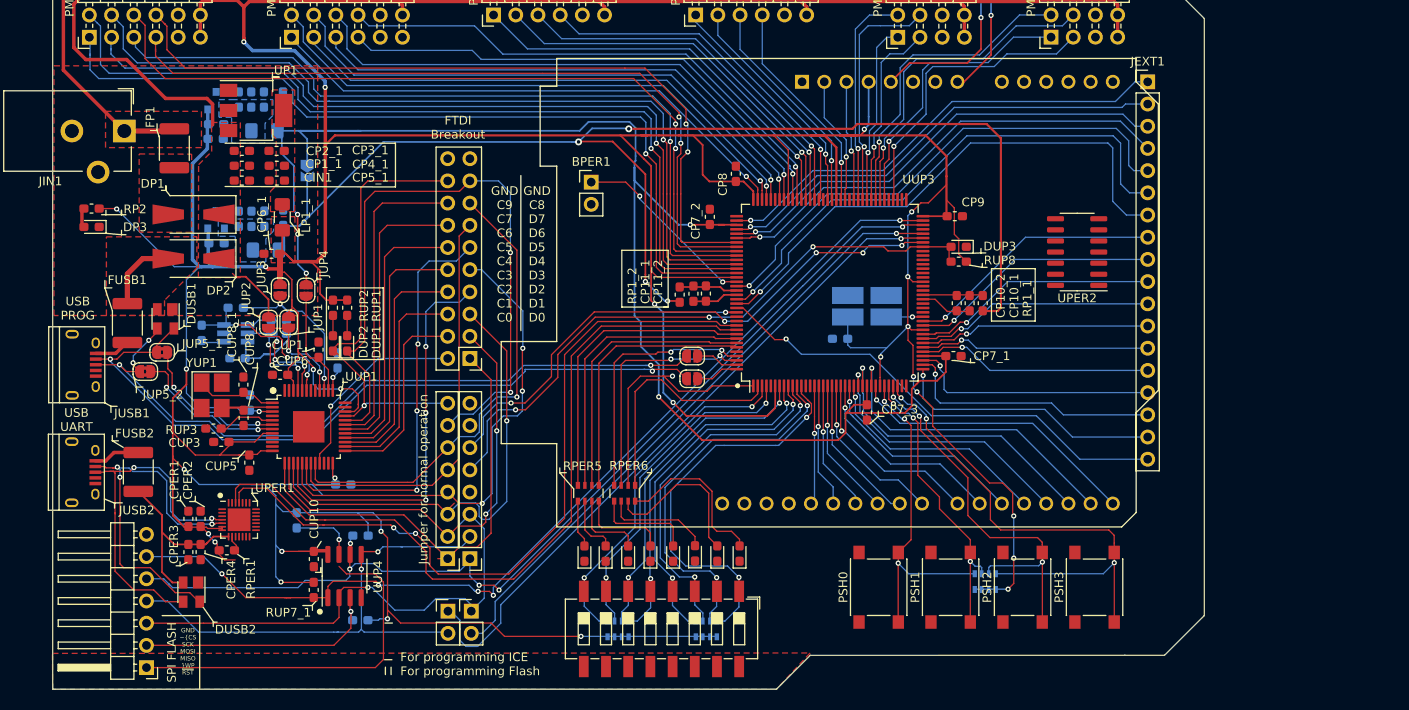
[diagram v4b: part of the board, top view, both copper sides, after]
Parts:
- added JEXT1: Conn_01x18-Connector_Generic, Connector_PinHeader_2.54mm:PinHeader_1x18_P2.54mm_Vertical, F.Cu at (209.6, 69.4)
- BPER1: footprint Buzzers_Beepers:Buzzer_12x9.5RM7.6 -> Connector_PinHeader_2.54mm:PinHeader_1x02_P2.54mm_Vertical
- CUP11, XUP1: moved to B.Cu
- moved BPER1 84.3 mm to (145.9, 80.8), turned to 0 degrees
- moved CUP11 29.9 mm to (174.4, 98.8), turned to 180 degrees
- moved XUP1 29.0 mm to (177.5, 95.0)
- moved UPER2 20.9 mm to (201.6, 88.8), turned to 180 degrees
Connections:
- UUP3 pad 112: Net-(UUP3-Pad112) -> /FPGA_IO/EXT2
- UUP3 pad 113: Net-(UUP3-Pad113) -> /FPGA_IO/EXT3
- UUP3 pad 114: Net-(UUP3-Pad114) -> /FPGA_IO/EXT4
- UUP3 pad 125: Net-(UUP3-Pad125) -> /FPGA_IO/EXT5
- UUP3 pad 128: Net-(UUP3-Pad128) -> /FPGA_IO/EXT6
- UUP3 pad 129: Net-(UUP3-Pad129) -> /FPGA_IO/EXT7
- UUP3 pad 130: Net-(UUP3-Pad130) -> /FPGA_IO/EXT18
- UUP3 pad 37: Net-(UUP3-Pad37) -> /FPGA_IO/EXT17
- UUP3 pad 38: Net-(UUP3-Pad38) -> /FPGA_IO/EXT16
- UUP3 pad 39: Net-(UUP3-Pad39) -> /FPGA_IO/EXT15
- UUP3 pad 41: Net-(UUP3-Pad41) -> /FPGA_IO/EXT14
- UUP3 pad 42: Net-(UUP3-Pad42) -> /FPGA_IO/EXT13
- UUP3 pad 43: Net-(UUP3-Pad43) -> /FPGA_IO/EXT12
- UUP3 pad 44: Net-(UUP3-Pad44) -> /FPGA_IO/EXT11
- UUP3 pad 45: Net-(UUP3-Pad45) -> /FPGA_IO/EXT10
- UUP3 pad 47: Net-(UUP3-Pad47) -> /FPGA_IO/EXT9
- UUP3 pad 48: Net-(UUP3-Pad48) -> /FPGA_IO/EXT8
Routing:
- net /VCC3V3: track 605.8 -> 733.9 mm, vias 20 -> 30
- net /FPGA_IO/EXT7: track 0.00 -> 62.4 mm, vias 0 -> 1
- net /FPGA_IO/EXT6: track 0.00 -> 61.1 mm, vias 0 -> 1
- net /FPGA_IO/EXT5: track 0.00 -> 59.1 mm, vias 0 -> 1
- net /FPGA_IO/EXT18: track 0.00 -> 54.3 mm, vias 0 -> 1
- net /FPGA_IO/EXT4: track 0.00 -> 53.9 mm, vias 0 -> 1
- net /FPGA_IO/EXT1: track 0.00 -> 53.6 mm, vias 0 -> 1
- net /FPGA_IO/EXT3: track 0.00 -> 53.3 mm, vias 0 -> 1
- net /FPGA_IO/EXT2: track 0.00 -> 53.0 mm, vias 0 -> 1
- net /FPGA_IO/EXT17: track 0.00 -> 30.9 mm, vias 0 -> 1
- net /FPGA_IO/EXT16: track 0.00 -> 30.1 mm, vias 0 -> 1
- net /FPGA_IO/EXT8: track 0.00 -> 29.7 mm, vias 0 -> 1
- net /FPGA_IO/EXT9: track 0.00 -> 28.8 mm, vias 0 -> 1
- net /FPGA_IO/EXT15: track 0.00 -> 28.7 mm, vias 0 -> 1
- net /FPGA_IO/EXT10: track 0.00 -> 28.2 mm, vias 0 -> 1
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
